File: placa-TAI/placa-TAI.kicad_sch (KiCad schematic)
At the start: 24 parts, among them J1 Screw_Terminal_01x02, J2 Screw_Terminal_01x02, J3 Conn_01x04_Female, J4 Conn_01x04_Male, J5 Screw_Terminal_01x02, SW1 SW_Push, SW2 SW_Push, U1 ESP-WROOM-02, U2 LM1117-3.3

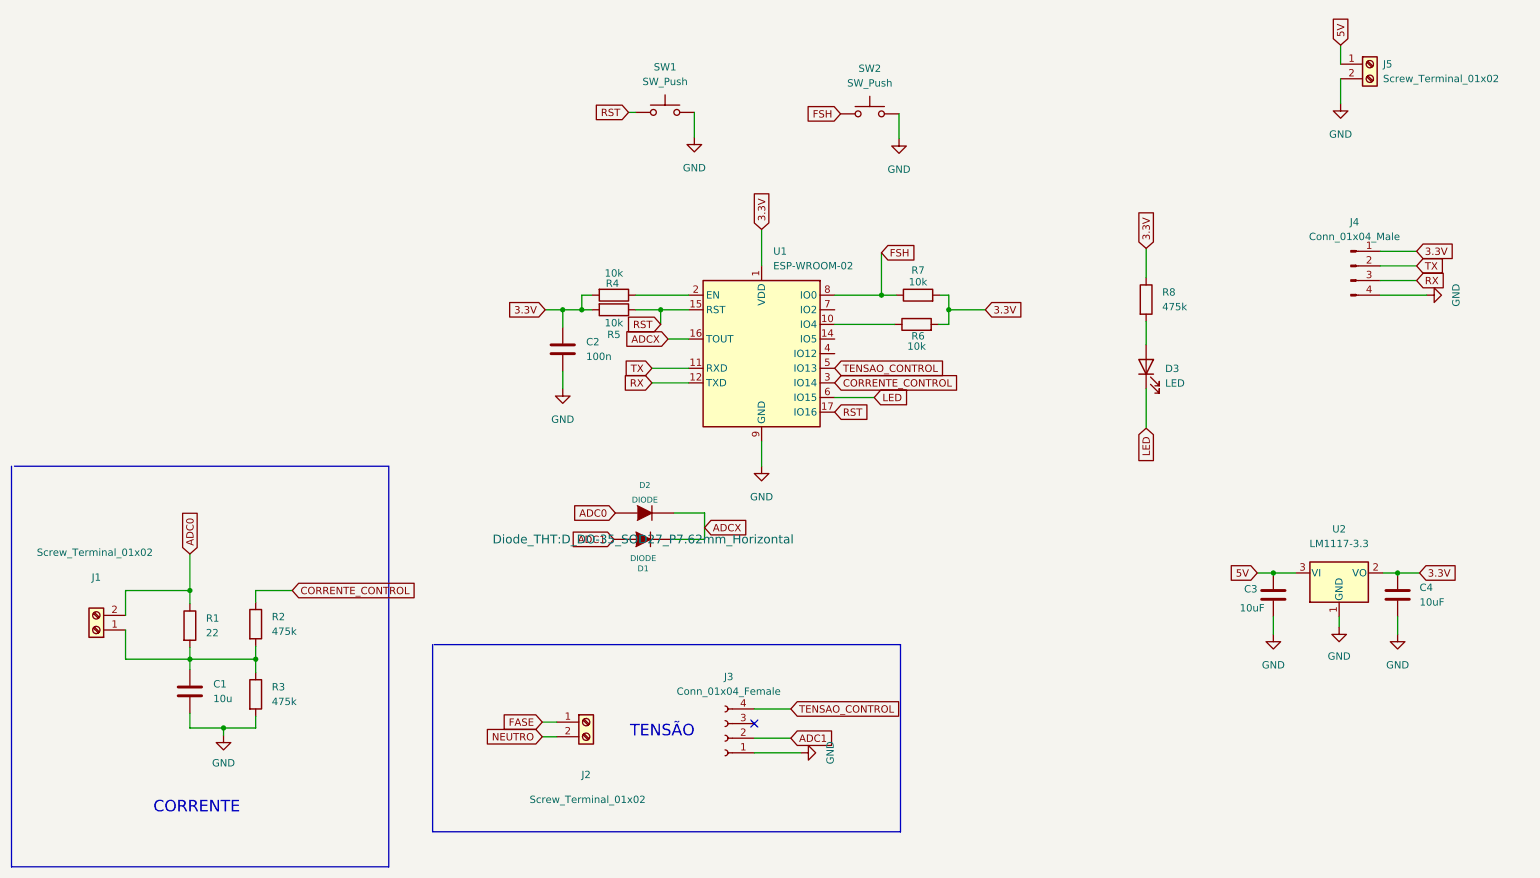
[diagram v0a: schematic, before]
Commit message: Add files via upload
Alterei o esp82 para o esp32
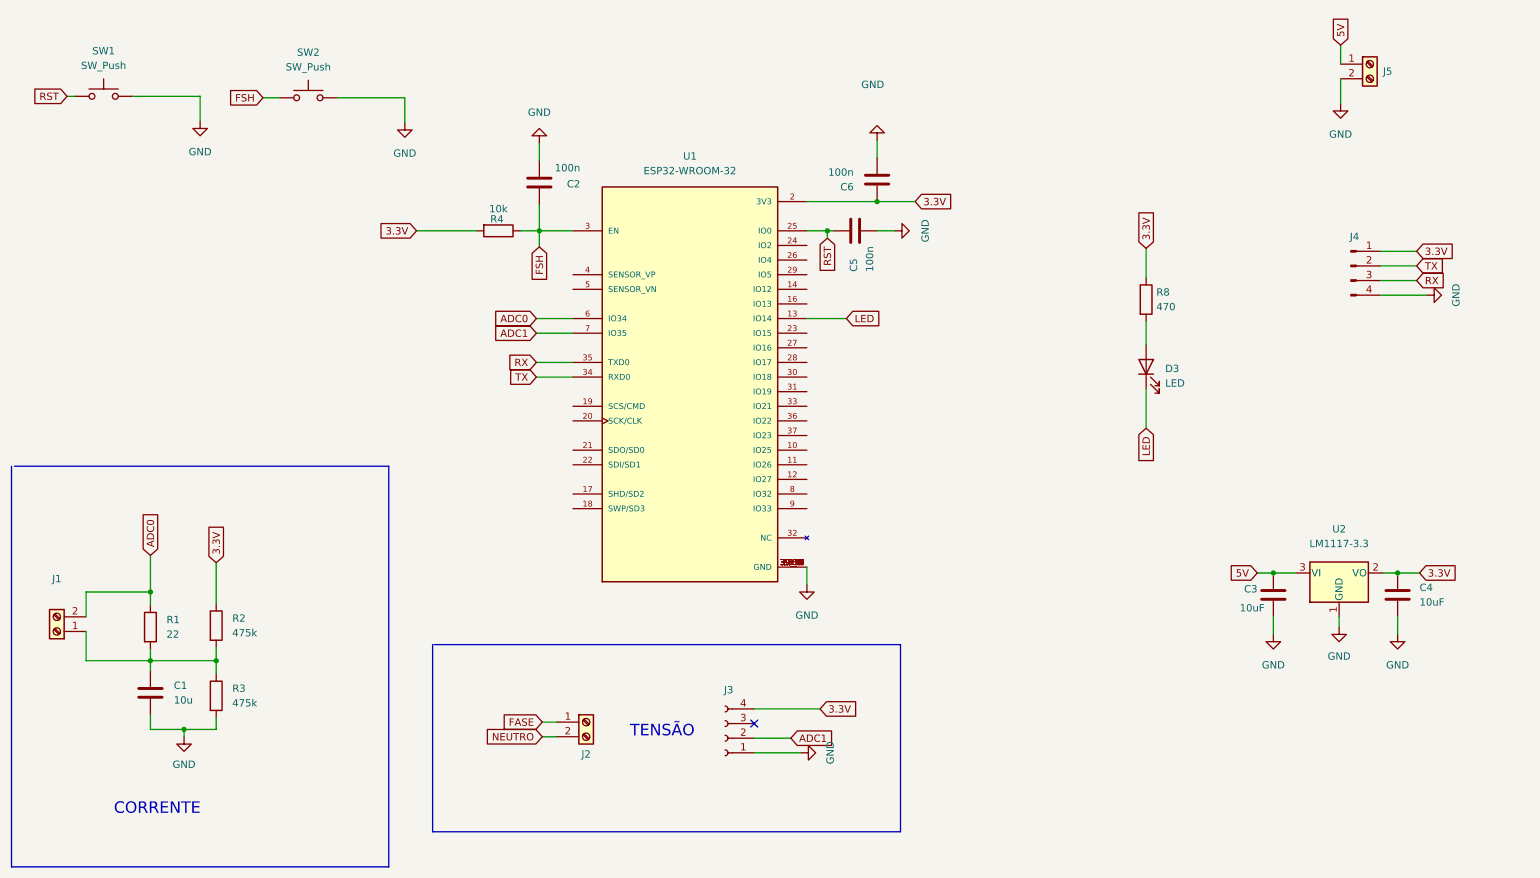
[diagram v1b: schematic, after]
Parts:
- removed D1, D2: DIODE, Diode_THT:D_DO-35_SOD27_P7.62mm_Horizontal, symbol max232:DIODE
- removed R5, R6, R7: 10k, Resistor_THT:R_Axial_DIN0207_L6.3mm_D2.5mm_P7.62mm_Horizontal, symbol Device:R
- removed U1: ESP-WROOM-02, RF_Module:ESP-WROOM-02, symbol RF_Module:ESP-WROOM-02
- added C5, C6: 100n, Capacitor_THT:CP_Radial_D10.0mm_P7.50mm, symbol Device:C
- added U1: ESP32-WROOM-32, esp32:MODULE_ESP32-WROOM-32, symbol ESP32-WROOM-32:ESP32-WROOM-32
- J1, J2, J5: footprint (none) -> Connector:JWT_A3963_1x02_P3.96mm_Vertical
- J3, J4: footprint (none) -> Connector_PinSocket_2.54mm:PinSocket_1x04_P2.54mm_Vertical
- R8: value 475k -> 470
- U2: footprint (none) -> TerminalBlock_Philmore:TerminalBlock_Philmore_TB133_1x03_P5.00mm_Horizontal
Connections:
- net CORRENTE_CONTROL is gone; now on net 3.3V: R2.1
- net TENSAO_CONTROL is gone; now on net 3.3V: J3.4 (Pin_4)
- net 3.3V: now also C6.1, U1.2 (3V3); no longer C2.1
- net ADC0: now also U1.6 (IO34)
- net ADC1: now also U1.7 (IO35)
- net FSH: now also C2.1, R4.1, U1.3 (EN)
- net GND: now also C5.2, C6.2, U1.1 (GND), U1.15 (GND), U1.38 (GND), U1.39_1 (GND), U1.39_10 (GND), U1.39_11 (GND), U1.39_12 (GND), U1.39_13 (GND), U1.39_14 (GND), U1.39_15 (GND), U1.39_16 (GND), U1.39_17 (GND), U1.39_18 (GND), U1.39_19 (GND), U1.39_2 (GND), U1.39_20 (GND), U1.39_21 (GND), U1.39_3 (GND), U1.39_4 (GND), U1.39_5 (GND), U1.39_6 (GND), U1.39_7 (GND), U1.39_8 (GND), U1.39_9 (GND)
- net LED: now also U1.13 (IO14)
- net RST: now also C5.1, U1.25 (IO0)
- net RX: now also U1.35 (TXD0)
- net TX: now also U1.34 (RXD0)
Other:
- moved on the sheet: C1, J1, R1, R2, R3, SW1, SW2
